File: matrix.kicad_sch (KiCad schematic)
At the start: 30 parts, among them SW10 SW_Push, SW11 SW_Push, SW12 SW_Push, SW13 SW_Push, SW14 SW_Push, SW15 SW_Push, SW16 SW_Push, SW2 SW_Push, SW3 SW_Push, SW4 SW_Push, SW5 SW_Push, SW6 SW_Push, SW7 SW_Push, SW8 SW_Push, SW9 SW_Push

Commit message: adjust paths for kicanvas
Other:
- company: (none) -> https://github.com/Challmymind
- title: (none) -> Keyboard based on STM32L0xx
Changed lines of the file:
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@@
 	(generator_version "8.0")
 	(paper "A4")
+	(title_block
+		(title "Keyboard based on STM32L0xx")
+		(date "2024-04-28")
+		(rev "0.1")
+		(company "https://github.com/Challmymind")
+	)
 	(junction
 		(at 161.29 78.74)

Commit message: completed 0.1 schematic design
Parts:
- D1, D10, D11, D12, D13, D14, D15, D2, D3, D4, D5, D6, D7, D8, D9: footprint (none) -> Diode_SMD:D_0805_2012Metric
- SW1: renamed from SW2; footprint (none) -> Button_Switch_Keyboard:SW_Cherry_MX_1.00u_PCB
- SW10: renamed from SW11; footprint (none) -> Button_Switch_Keyboard:SW_Cherry_MX_1.00u_PCB
- SW11: renamed from SW12; footprint (none) -> Button_Switch_Keyboard:SW_Cherry_MX_1.00u_PCB
- SW12: renamed from SW13; footprint (none) -> Button_Switch_Keyboard:SW_Cherry_MX_1.00u_PCB
- SW13: renamed from SW14; footprint (none) -> Button_Switch_Keyboard:SW_Cherry_MX_1.00u_PCB
- SW14: renamed from SW15; footprint (none) -> Button_Switch_Keyboard:SW_Cherry_MX_1.00u_PCB
- SW15: renamed from SW16; footprint (none) -> Button_Switch_Keyboard:SW_Cherry_MX_1.00u_PCB
- SW2: renamed from SW3; footprint (none) -> Button_Switch_Keyboard:SW_Cherry_MX_1.00u_PCB
- SW3: renamed from SW4; footprint (none) -> Button_Switch_Keyboard:SW_Cherry_MX_1.00u_PCB
- SW4: renamed from SW5; footprint (none) -> Button_Switch_Keyboard:SW_Cherry_MX_1.00u_PCB
- SW5: renamed from SW6; footprint (none) -> Button_Switch_Keyboard:SW_Cherry_MX_1.00u_PCB
- SW6: renamed from SW7; footprint (none) -> Button_Switch_Keyboard:SW_Cherry_MX_1.00u_PCB
- SW7: renamed from SW8; footprint (none) -> Button_Switch_Keyboard:SW_Cherry_MX_1.00u_PCB
- SW8: renamed from SW9; footprint (none) -> Button_Switch_Keyboard:SW_Cherry_MX_1.00u_PCB
- SW9: renamed from SW10; footprint (none) -> Button_Switch_Keyboard:SW_Cherry_MX_1.00u_PCB
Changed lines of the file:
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@@
 			)
 		)
-		(property "Footprint" ""
+		(property "Footprint" "Diode_SMD:D_0805_2012Metric"
 			(at 165.1 119.38 0)
 			(effects
@@
 			)
 		)
-		(property "Footprint" ""
+		(property "Footprint" "Diode_SMD:D_0805_2012Metric"
 			(at 149.86 119.38 0)
 			(effects
@@
 			)
 		)
-		(property "Footprint" ""
+		(property "Footprint" "Diode_SMD:D_0805_2012Metric"
 			(at 165.1 83.82 0)
 			(effects
@@
 		(on_board yes)
 		(dnp no)
-		(property "Reference" "SW7"
+		(property "Reference" "SW6"
 			(at 125.73 92.456 0)
 			(effects
@@
 			)
 		)
-		(property "Footprint" ""
+		(property "Footprint" "Button_Switch_Keyboard:SW_Cherry_MX_1.00u_PCB"
 			(at 125.73 91.44 0)
 			(effects
@@
 			(project "stm_skeyboard"
 				(path "/f8cbad95-1fac-4ee0-b4c1-fc27b4678331/471ebd7f-24aa-4a86-aa3a-deafb21e0afc"
-					(reference "SW7")
+					(reference "SW6")
 					(unit 1)
 				)
@@
 			)
 		)
-		(property "Footprint" ""
+		(property "Footprint" "Diode_SMD:D_0805_2012Metric"
 			(at 149.86 101.6 0)
 			(effects
@@
 		(on_board yes)
 		(dnp no)
-		(property "Reference" "SW16"
+		(property "Reference" "SW15"
 			(at 186.69 109.982 0)
 			(effects
@@
 			)
 		)
-		(property "Footprint" ""
+		(property "Footprint" "Button_Switch_Keyboard:SW_Cherry_MX_1.00u_PCB"
 			(at 186.69 109.22 0)
 			(effects
@@
 			(project "stm_skeyboard"
 				(path "/f8cbad95-1fac-4ee0-b4c1-fc27b4678331/471ebd7f-24aa-4a86-aa3a-deafb21e0afc"
-					(reference "SW16")
+					(reference "SW15")
 					(unit 1)
 				)
@@
 			)
 		)
-		(property "Footprint" ""
+		(property "Footprint" "Diode_SMD:D_0805_2012Metric"
 			(at 134.62 119.38 0)
 			(effects
@@
 		(on_board yes)
 		(dnp no)
-		(property "Reference" "SW13"
+		(property "Reference" "SW12"
 			(at 140.97 110.49 0)
 			(effects
@@
 			)
 		)
-		(property "Footprint" ""
+		(property "Footprint" "Button_Switch_Keyboard:SW_Cherry_MX_1.00u_PCB"
 			(at 140.97 109.22 0)
 			(effects
@@
 			(project "stm_skeyboard"
 				(path "/f8cbad95-1fac-4ee0-b4c1-fc27b4678331/471ebd7f-24aa-4a86-aa3a-deafb21e0afc"
-					(reference "SW13")
+					(reference "SW12")
 					(unit 1)
 				)
@@
 		(on_board yes)
 		(dnp no)
-		(property "Reference" "SW14"
+		(property "Reference" "SW13"
 			(at 156.21 109.982 0)
 			(effects
@@
 			)
 		)
-		(property "Footprint" ""
+		(property "Footprint" "Button_Switch_Keyboard:SW_Cherry_MX_1.00u_PCB"
 			(at 156.21 109.22 0)
 			(effects
@@
 			(project "stm_skeyboard"
 				(path "/f8cbad95-1fac-4ee0-b4c1-fc27b4678331/471ebd7f-24aa-4a86-aa3a-deafb21e0afc"
-					(reference "SW14")
+					(reference "SW13")
 					(unit 1)
 				)
@@
 			)
 		)
-		(property "Footprint" ""
+		(property "Footprint" "Diode_SMD:D_0805_2012Metric"
 			(at 180.34 83.82 0)
 			(effects
@@
 			)
 		)
-		(property "Footprint" ""
+		(property "Footprint" "Diode_SMD:D_0805_2012Metric"
 			(at 134.62 83.82 0)
 			(effects
@@
 		(on_board yes)
 		(dnp no)
-		(property "Reference" "SW5"
+		(property "Reference" "SW4"
 			(at 171.45 74.676 0)
 			(effects
@@
 			)
 		)
-		(property "Footprint" ""
+		(property "Footprint" "Button_Switch_Keyboard:SW_Cherry_MX_1.00u_PCB"
 			(at 171.45 73.66 0)
 			(effects
@@
 			(project "stm_skeyboard"
 				(path "/f8cbad95-1fac-4ee0-b4c1-fc27b4678331/471ebd7f-24aa-4a86-aa3a-deafb21e0afc"
-					(reference "SW5")
+					(reference "SW4")
 					(unit 1)
 				)
@@
 			)
 		)
-		(property "Footprint" ""
+		(property "Footprint" "Diode_SMD:D_0805_2012Metric"
 			(at 165.1 101.6 0)
 			(effects
@@
 		(on_board yes)
 		(dnp no)
-		(property "Reference" "SW6"
+		(property "Reference" "SW5"
 			(at 186.69 74.422 0)
 			(effects
@@
 			)
 		)
-		(property "Footprint" ""
+		(property "Footprint" "Button_Switch_Keyboard:SW_Cherry_MX_1.00u_PCB"
 			(at 186.69 73.66 0)
 			(effects
@@
 			(project "stm_skeyboard"
 				(path "/f8cbad95-1fac-4ee0-b4c1-fc27b4678331/471ebd7f-24aa-4a86-aa3a-deafb21e0afc"
-					(reference "SW6")
+					(reference "SW5")
 					(unit 1)
 				)
@@
 			)
 		)
-		(property "Footprint" ""
+		(property "Footprint" "Diode_SMD:D_0805_2012Metric"
 			(at 180.34 101.6 0)
 			(effects
@@
 		(on_board yes)
 		(dnp no)
-		(property "Reference" "SW2"
+		(property "Reference" "SW1"
 			(at 125.73 74.676 0)
 			(effects
@@
 			)
 		)
-		(property "Footprint" ""
+		(property "Footprint" "Button_Switch_Keyboard:SW_Cherry_MX_1.00u_PCB"
 			(at 125.73 73.66 0)
 			(effects
@@
 			(project "stm_skeyboard"
 				(path "/f8cbad95-1fac-4ee0-b4c1-fc27b4678331/471ebd7f-24aa-4a86-aa3a-deafb21e0afc"
-					(reference "SW2")
+					(reference "SW1")
 					(unit 1)
 				)
@@
 			)
 		)
-		(property "Footprint" ""
+		(property "Footprint" "Diode_SMD:D_0805_2012Metric"
 			(at 134.62 101.6 0)
 			(effects
@@
 		(on_board yes)
 		(dnp no)
-		(property "Reference" "SW12"
+		(property "Reference" "SW11"
 			(at 125.73 110.236 0)
 			(effects
@@
 			)
 		)
-		(property "Footprint" ""
+		(property "Footprint" "Button_Switch_Keyboard:SW_Cherry_MX_1.00u_PCB"
 			(at 125.73 109.22 0)
 			(effects
@@
 			(project "stm_skeyboard"
 				(path "/f8cbad95-1fac-4ee0-b4c1-fc27b4678331/471ebd7f-24aa-4a86-aa3a-deafb21e0afc"
-					(reference "SW12")
+					(reference "SW11")
 					(unit 1)
 				)
@@
 			)
 		)
-		(property "Footprint" ""
+		(property "Footprint" "Diode_SMD:D_0805_2012Metric"
 			(at 149.86 83.82 0)
 			(effects
@@
 			)
 		)
-		(property "Footprint" ""
+		(property "Footprint" "Diode_SMD:D_0805_2012Metric"
 			(at 119.38 119.38 0)
 			(effects
@@
 		(on_board yes)
 		(dnp no)
-		(property "Reference" "SW9"
+		(property "Reference" "SW8"
 			(at 156.21 92.202 0)
 			(effects
@@
 			)
 		)
-		(property "Footprint" ""
+		(property "Footprint" "Button_Switch_Keyboard:SW_Cherry_MX_1.00u_PCB"
 			(at 156.21 91.44 0)
 			(effects
@@
 			(project "stm_skeyboard"
 				(path "/f8cbad95-1fac-4ee0-b4c1-fc27b4678331/471ebd7f-24aa-4a86-aa3a-deafb21e0afc"
-					(reference "SW9")
+					(reference "SW8")
 					(unit 1)
 				)
@@
 		(on_board yes)
 		(dnp no)
-		(property "Reference" "SW15"
+		(property "Reference" "SW14"
 			(at 171.45 110.236 0)
 			(effects
@@
 			)
 		)
-		(property "Footprint" ""
+		(property "Footprint" "Button_Switch_Keyboard:SW_Cherry_MX_1.00u_PCB"
 			(at 171.45 109.22 0)
 			(effects
@@
 			(project "stm_skeyboard"
 				(path "/f8cbad95-1fac-4ee0-b4c1-fc27b4678331/471ebd7f-24aa-4a86-aa3a-deafb21e0afc"
-					(reference "SW15")
+					(reference "SW14")
 					(unit 1)
 				)
@@
 		(on_board yes)
 		(dnp no)
-		(property "Reference" "SW8"
+		(property "Reference" "SW7"
 			(at 140.97 92.71 0)
 			(effects
@@
 			)
 		)
-		(property "Footprint" ""
+		(property "Footprint" "Button_Switch_Keyboard:SW_Cherry_MX_1.00u_PCB"
 			(at 140.97 91.44 0)
 			(effects
@@
 			(project "stm_skeyboard"
 				(path "/f8cbad95-1fac-4ee0-b4c1-fc27b4678331/471ebd7f-24aa-4a86-aa3a-deafb21e0afc"
-					(reference "SW8")
+					(reference "SW7")
 					(unit 1)
 				)
@@
 		(on_board yes)
 		(dnp no)
-		(property "Reference" "SW10"
+		(property "Reference" "SW9"
 			(at 171.45 92.456 0)
 			(effects
@@
 			)
 		)
-		(property "Footprint" ""
+		(property "Footprint" "Button_Switch_Keyboard:SW_Cherry_MX_1.00u_PCB"
 			(at 171.45 91.44 0)
 			(effects
@@
 			(project "stm_skeyboard"
 				(path "/f8cbad95-1fac-4ee0-b4c1-fc27b4678331/471ebd7f-24aa-4a86-aa3a-deafb21e0afc"
-					(reference "SW10")
+					(reference "SW9")
 					(unit 1)
 				)
@@
 		(on_board yes)
 		(dnp no)
-		(property "Reference" "SW11"
+		(property "Reference" "SW10"
 			(at 186.69 92.202 0)
 			(effects
@@
 			)
 		)
-		(property "Footprint" ""
+		(property "Footprint" "Button_Switch_Keyboard:SW_Cherry_MX_1.00u_PCB"
 			(at 186.69 91.44 0)
 			(effects
@@
 			(project "stm_skeyboard"
 				(path "/f8cbad95-1fac-4ee0-b4c1-fc27b4678331/471ebd7f-24aa-4a86-aa3a-deafb21e0afc"
-					(reference "SW11")
+					(reference "SW10")
 					(unit 1)
 				)
@@
 			)
 		)
-		(property "Footprint" ""
+		(property "Footprint" "Diode_SMD:D_0805_2012Metric"
 			(at 119.38 101.6 0)
 			(effects
@@
 		(on_board yes)
 		(dnp no)
-		(property "Reference" "SW3"
+		(property "Reference" "SW2"
 			(at 140.97 74.93 0)
 			(effects
@@
 			)
 		)
-		(property "Footprint" ""
+		(property "Footprint" "Button_Switch_Keyboard:SW_Cherry_MX_1.00u_PCB"
 			(at 140.97 73.66 0)
 			(effects
@@
 			(project "stm_skeyboard"
 				(path "/f8cbad95-1fac-4ee0-b4c1-fc27b4678331/471ebd7f-24aa-4a86-aa3a-deafb21e0afc"
-					(reference "SW3")
+					(reference "SW2")
 					(unit 1)
 				)
@@
 			)
 		)
-		(property "Footprint" ""
+		(property "Footprint" "Diode_SMD:D_0805_2012Metric"
 			(at 119.38 83.82 0)
 			(effects
@@
 			)
 		)
-		(property "Footprint" ""
+		(property "Footprint" "Diode_SMD:D_0805_2012Metric"
 			(at 180.34 119.38 0)
 			(effects
@@
 		(on_board yes)
 		(dnp no)
-		(property "Reference" "SW4"
+		(property "Reference" "SW3"
 			(at 156.21 74.422 0)
 			(effects
@@
 			)
 		)
-		(property "Footprint" ""
+		(property "Footprint" "Button_Switch_Keyboard:SW_Cherry_MX_1.00u_PCB"
 			(at 156.21 73.66 0)
 			(effects
@@
 			(project "stm_skeyboard"
 				(path "/f8cbad95-1fac-4ee0-b4c1-fc27b4678331/471ebd7f-24aa-4a86-aa3a-deafb21e0afc"
-					(reference "SW4")
-					(unit 1)
-				)
+					(reference "SW3")
+					(unit 1)
+				)

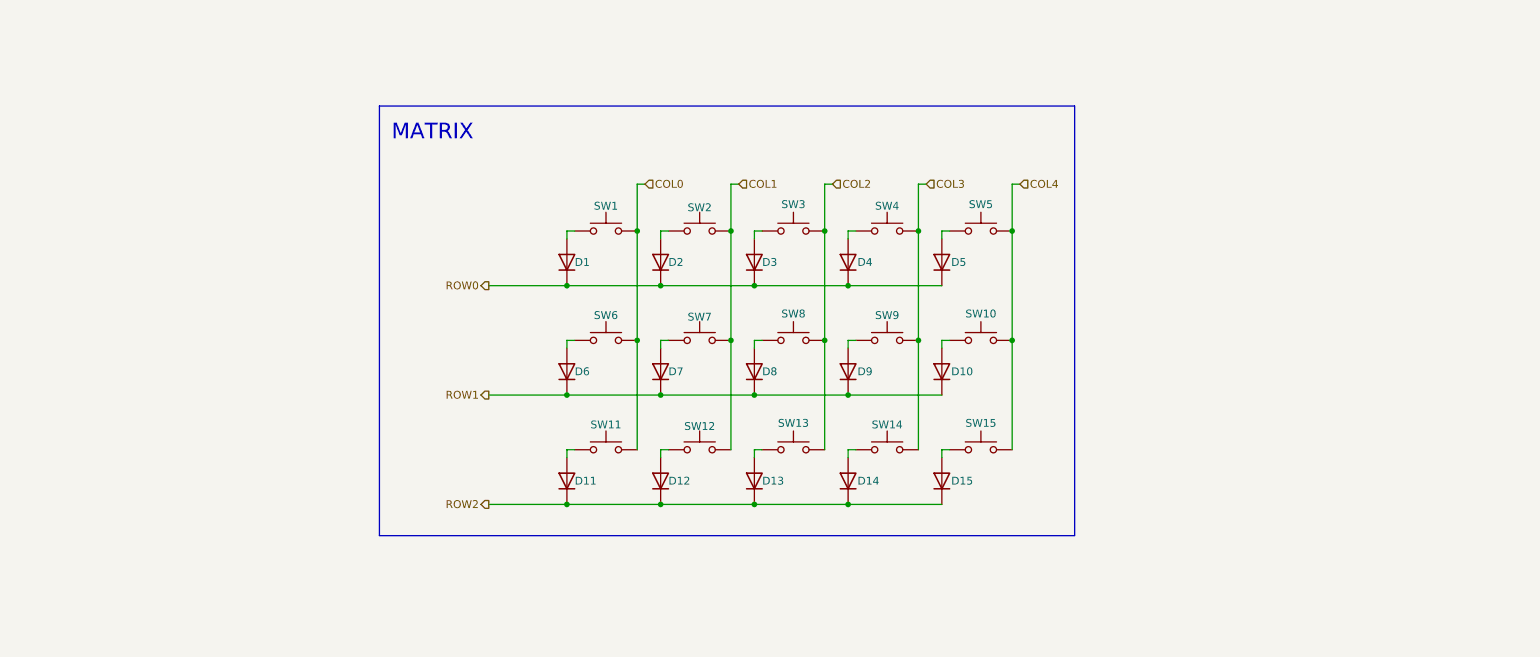
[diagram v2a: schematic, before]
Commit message: switched to bigger matrix, adjusted mcu pins, started pcb layout
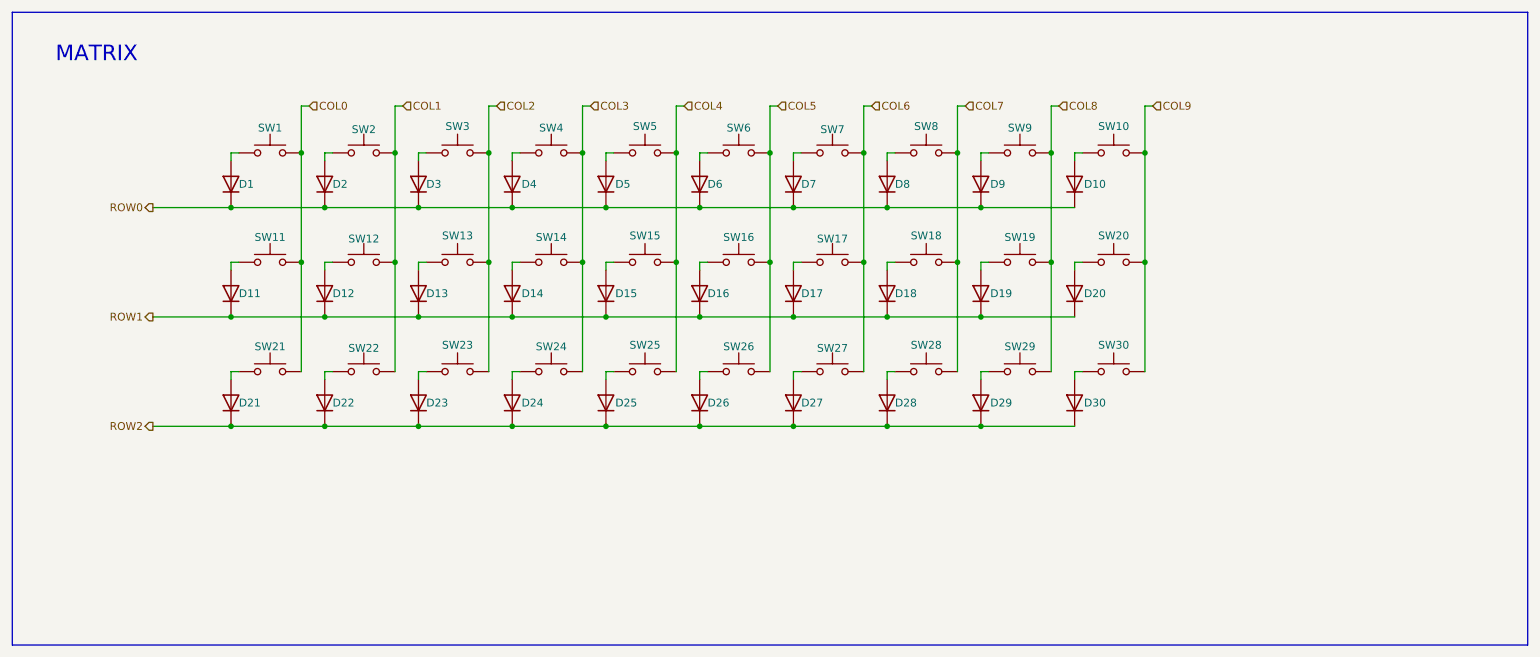
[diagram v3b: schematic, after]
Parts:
- added D10, D16, D17, D18, D19, D20, D26, D27, D28, D29, D30, D6, D7, D8, D9: D, Diode_SMD:D_0805_2012Metric, symbol Device:D
- added SW10, SW16, SW17, SW18, SW19, SW20, SW26, SW27, SW28, SW29, SW30, SW6, SW7, SW8, SW9: SW_Push, Button_Switch_Keyboard:SW_Cherry_MX_1.00u_PCB, symbol Switch:SW_Push
- renumbered D6 to D11, D7 to D12, D8 to D13, D9 to D14, D10 to D15, D11 to D21, D12 to D22, D13 to D23, D14 to D24, D15 to D25, SW6 to SW11, SW7 to SW12, SW8 to SW13, SW9 to SW14, SW10 to SW15, SW11 to SW21, SW12 to SW22, SW13 to SW23, SW14 to SW24, SW15 to SW25
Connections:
- net ROW0: now also D10.1 (K), D6.1 (K), D7.1 (K), D8.1 (K), D9.1 (K)
- net ROW1: now also D16.1 (K), D17.1 (K), D18.1 (K), D19.1 (K), D20.1 (K)
- net ROW2: now also D26.1 (K), D27.1 (K), D28.1 (K), D29.1 (K), D30.1 (K)
- new net: D16.2 (A), SW16.1
- new net: D20.2 (A), SW20.1
- new net: D18.2 (A), SW18.1
- new net: D30.2 (A), SW30.1
- new net: D28.2 (A), SW28.1
- new net: D26.2 (A), SW26.1
- new net: D6.2 (A), SW6.1
- new net: D9.2 (A), SW9.1
- new net: D17.2 (A), SW17.1
- new net: D29.2 (A), SW29.1
- new net: D27.2 (A), SW27.1
- new net: D8.2 (A), SW8.1
- new net: D19.2 (A), SW19.1
- new net: D10.2 (A), SW10.1
- new net: D7.2 (A), SW7.1
- new net COL5: SW16.2, SW26.2, SW6.2
- new net COL6: SW17.2, SW27.2, SW7.2
- new net COL7: SW18.2, SW28.2, SW8.2
- new net COL8: SW19.2, SW29.2, SW9.2
- new net COL9: SW10.2, SW20.2, SW30.2
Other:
- moved on the sheet: D1, D11, D12, D13, D14, D15, D2, D21, D22, D23, D24, D25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

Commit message: added 3d models, completed 0.1
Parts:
- SW1, SW10, SW11, SW12, SW13, SW14, SW15, SW16, SW17, SW18, SW19, SW2, SW20, SW21, SW22, SW23, SW24, SW25, SW26, SW27, SW28, SW29, SW3, SW30, SW4, SW5, SW6, SW7, SW8, SW9: footprint Button_Switch_Keyboard:SW_Cherry_MX_1.00u_PCB -> my_switch:SW_Cherry_MX_1.00u_PCB
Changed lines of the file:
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@@
 			)
 		)
-		(property "Footprint" "Button_Switch_Keyboard:SW_Cherry_MX_1.00u_PCB"
+		(property "Footprint" "my_switch:SW_Cherry_MX_1.00u_PCB"
 			(at 147.32 78.74 0)
 			(effects
@@
 			)
 		)
-		(property "Footprint" "Button_Switch_Keyboard:SW_Cherry_MX_1.00u_PCB"
+		(property "Footprint" "my_switch:SW_Cherry_MX_1.00u_PCB"
 			(at 71.12 78.74 0)
 			(effects
@@
 			)
 		)
-		(property "Footprint" "Button_Switch_Keyboard:SW_Cherry_MX_1.00u_PCB"
+		(property "Footprint" "my_switch:SW_Cherry_MX_1.00u_PCB"
 			(at 208.28 96.52 0)
 			(effects
@@
 			)
 		)
-		(property "Footprint" "Button_Switch_Keyboard:SW_Cherry_MX_1.00u_PCB"
+		(property "Footprint" "my_switch:SW_Cherry_MX_1.00u_PCB"
 			(at 147.32 60.96 0)
 			(effects
@@
 			)
 		)
-		(property "Footprint" "Button_Switch_Keyboard:SW_Cherry_MX_1.00u_PCB"
+		(property "Footprint" "my_switch:SW_Cherry_MX_1.00u_PCB"
 			(at 193.04 60.96 0)
 			(effects
@@
 			)
 		)
-		(property "Footprint" "Button_Switch_Keyboard:SW_Cherry_MX_1.00u_PCB"
+		(property "Footprint" "my_switch:SW_Cherry_MX_1.00u_PCB"
 			(at 162.56 78.74 0)
 			(effects
@@
 			)
 		)
-		(property "Footprint" "Button_Switch_Keyboard:SW_Cherry_MX_1.00u_PCB"
+		(property "Footprint" "my_switch:SW_Cherry_MX_1.00u_PCB"
 			(at 132.08 96.52 0)
 			(effects
@@
 			)
 		)
-		(property "Footprint" "Button_Switch_Keyboard:SW_Cherry_MX_1.00u_PCB"
+		(property "Footprint" "my_switch:SW_Cherry_MX_1.00u_PCB"
 			(at 193.04 78.74 0)
 			(effects
@@
 			)
 		)
-		(property "Footprint" "Button_Switch_Keyboard:SW_Cherry_MX_1.00u_PCB"
+		(property "Footprint" "my_switch:SW_Cherry_MX_1.00u_PCB"
 			(at 86.36 96.52 0)
 			(effects
@@
 			)
 		)
-		(property "Footprint" "Button_Switch_Keyboard:SW_Cherry_MX_1.00u_PCB"
+		(property "Footprint" "my_switch:SW_Cherry_MX_1.00u_PCB"
 			(at 101.6 96.52 0)
 			(effects
@@
 			)
 		)
-		(property "Footprint" "Button_Switch_Keyboard:SW_Cherry_MX_1.00u_PCB"
+		(property "Footprint" "my_switch:SW_Cherry_MX_1.00u_PCB"
 			(at 177.8 96.52 0)
 			(effects
@@
 			)
 		)
-		(property "Footprint" "Button_Switch_Keyboard:SW_Cherry_MX_1.00u_PCB"
+		(property "Footprint" "my_switch:SW_Cherry_MX_1.00u_PCB"
 			(at 208.28 78.74 0)
 			(effects
@@
 			)
 		)
-		(property "Footprint" "Button_Switch_Keyboard:SW_Cherry_MX_1.00u_PCB"
+		(property "Footprint" "my_switch:SW_Cherry_MX_1.00u_PCB"
 			(at 177.8 78.74 0)
 			(effects
@@
 			)
 		)
-		(property "Footprint" "Button_Switch_Keyboard:SW_Cherry_MX_1.00u_PCB"
+		(property "Footprint" "my_switch:SW_Cherry_MX_1.00u_PCB"
 			(at 116.84 60.96 0)
 			(effects
@@
 			)
 		)
-		(property "Footprint" "Button_Switch_Keyboard:SW_Cherry_MX_1.00u_PCB"
+		(property "Footprint" "my_switch:SW_Cherry_MX_1.00u_PCB"
 			(at 132.08 60.96 0)
 			(effects
@@
 			)
 		)
-		(property "Footprint" "Button_Switch_Keyboard:SW_Cherry_MX_1.00u_PCB"
+		(property "Footprint" "my_switch:SW_Cherry_MX_1.00u_PCB"
 			(at 71.12 60.96 0)
 			(effects
@@
 			)
 		)
-		(property "Footprint" "Button_Switch_Keyboard:SW_Cherry_MX_1.00u_PCB"
+		(property "Footprint" "my_switch:SW_Cherry_MX_1.00u_PCB"
 			(at 71.12 96.52 0)
 			(effects
@@
 			)
 		)
-		(property "Footprint" "Button_Switch_Keyboard:SW_Cherry_MX_1.00u_PCB"
+		(property "Footprint" "my_switch:SW_Cherry_MX_1.00u_PCB"
 			(at 193.04 96.52 0)
 			(effects
@@
 			)
 		)
-		(property "Footprint" "Button_Switch_Keyboard:SW_Cherry_MX_1.00u_PCB"
+		(property "Footprint" "my_switch:SW_Cherry_MX_1.00u_PCB"
 			(at 101.6 78.74 0)
 			(effects
@@
 			)
 		)
-		(property "Footprint" "Button_Switch_Keyboard:SW_Cherry_MX_1.00u_PCB"
+		(property "Footprint" "my_switch:SW_Cherry_MX_1.00u_PCB"
 			(at 208.28 60.96 0)
 			(effects
@@
 			)
 		)
-		(property "Footprint" "Button_Switch_Keyboard:SW_Cherry_MX_1.00u_PCB"
+		(property "Footprint" "my_switch:SW_Cherry_MX_1.00u_PCB"
 			(at 116.84 96.52 0)
 			(effects
@@
 			)
 		)
-		(property "Footprint" "Button_Switch_Keyboard:SW_Cherry_MX_1.00u_PCB"
+		(property "Footprint" "my_switch:SW_Cherry_MX_1.00u_PCB"
 			(at 86.36 78.74 0)
 			(effects
@@
 			)
 		)
-		(property "Footprint" "Button_Switch_Keyboard:SW_Cherry_MX_1.00u_PCB"
+		(property "Footprint" "my_switch:SW_Cherry_MX_1.00u_PCB"
 			(at 147.32 96.52 0)
 			(effects
@@
 			)
 		)
-		(property "Footprint" "Button_Switch_Keyboard:SW_Cherry_MX_1.00u_PCB"
+		(property "Footprint" "my_switch:SW_Cherry_MX_1.00u_PCB"
 			(at 177.8 60.96 0)
 			(effects
@@
 			)
 		)
-		(property "Footprint" "Button_Switch_Keyboard:SW_Cherry_MX_1.00u_PCB"
+		(property "Footprint" "my_switch:SW_Cherry_MX_1.00u_PCB"
 			(at 116.84 78.74 0)
 			(effects
@@
 			)
 		)
-		(property "Footprint" "Button_Switch_Keyboard:SW_Cherry_MX_1.00u_PCB"
+		(property "Footprint" "my_switch:SW_Cherry_MX_1.00u_PCB"
 			(at 162.56 96.52 0)
 			(effects
@@
 			)
 		)
-		(property "Footprint" "Button_Switch_Keyboard:SW_Cherry_MX_1.00u_PCB"
+		(property "Footprint" "my_switch:SW_Cherry_MX_1.00u_PCB"
 			(at 162.56 60.96 0)
 			(effects
@@
 			)
 		)
-		(property "Footprint" "Button_Switch_Keyboard:SW_Cherry_MX_1.00u_PCB"
+		(property "Footprint" "my_switch:SW_Cherry_MX_1.00u_PCB"
 			(at 132.08 78.74 0)
 			(effects
@@
 			)
 		)
-		(property "Footprint" "Button_Switch_Keyboard:SW_Cherry_MX_1.00u_PCB"
+		(property "Footprint" "my_switch:SW_Cherry_MX_1.00u_PCB"
 			(at 86.36 60.96 0)
 			(effects
@@
 			)
 		)
-		(property "Footprint" "Button_Switch_Keyboard:SW_Cherry_MX_1.00u_PCB"
+		(property "Footprint" "my_switch:SW_Cherry_MX_1.00u_PCB"
 			(at 101.6 60.96 0)
 			(effects
